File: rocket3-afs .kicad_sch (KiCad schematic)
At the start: 98 parts, among them IC1 ISL85005AFRZ-T7A, J1 ARMING_PLUG, J2 POWER, J3 E-MATCH_DROGUE, J4 SWD, J5 E-MATCH_RECOVERY, M5 MG90S, M6 MG90S, M7 MG90S, M8 MG90s, Q1 Q_NMOS_GSD, Q2 Q_NMOS_GSD, Q3 Q_NMOS_GSD, Q4 Q_NMOS_GSD, Q6 BC547, U2 MP1584EN-LF-Z, U8 USBLC6-2SC6, U9 MMC5983MA, Y1 16MHz

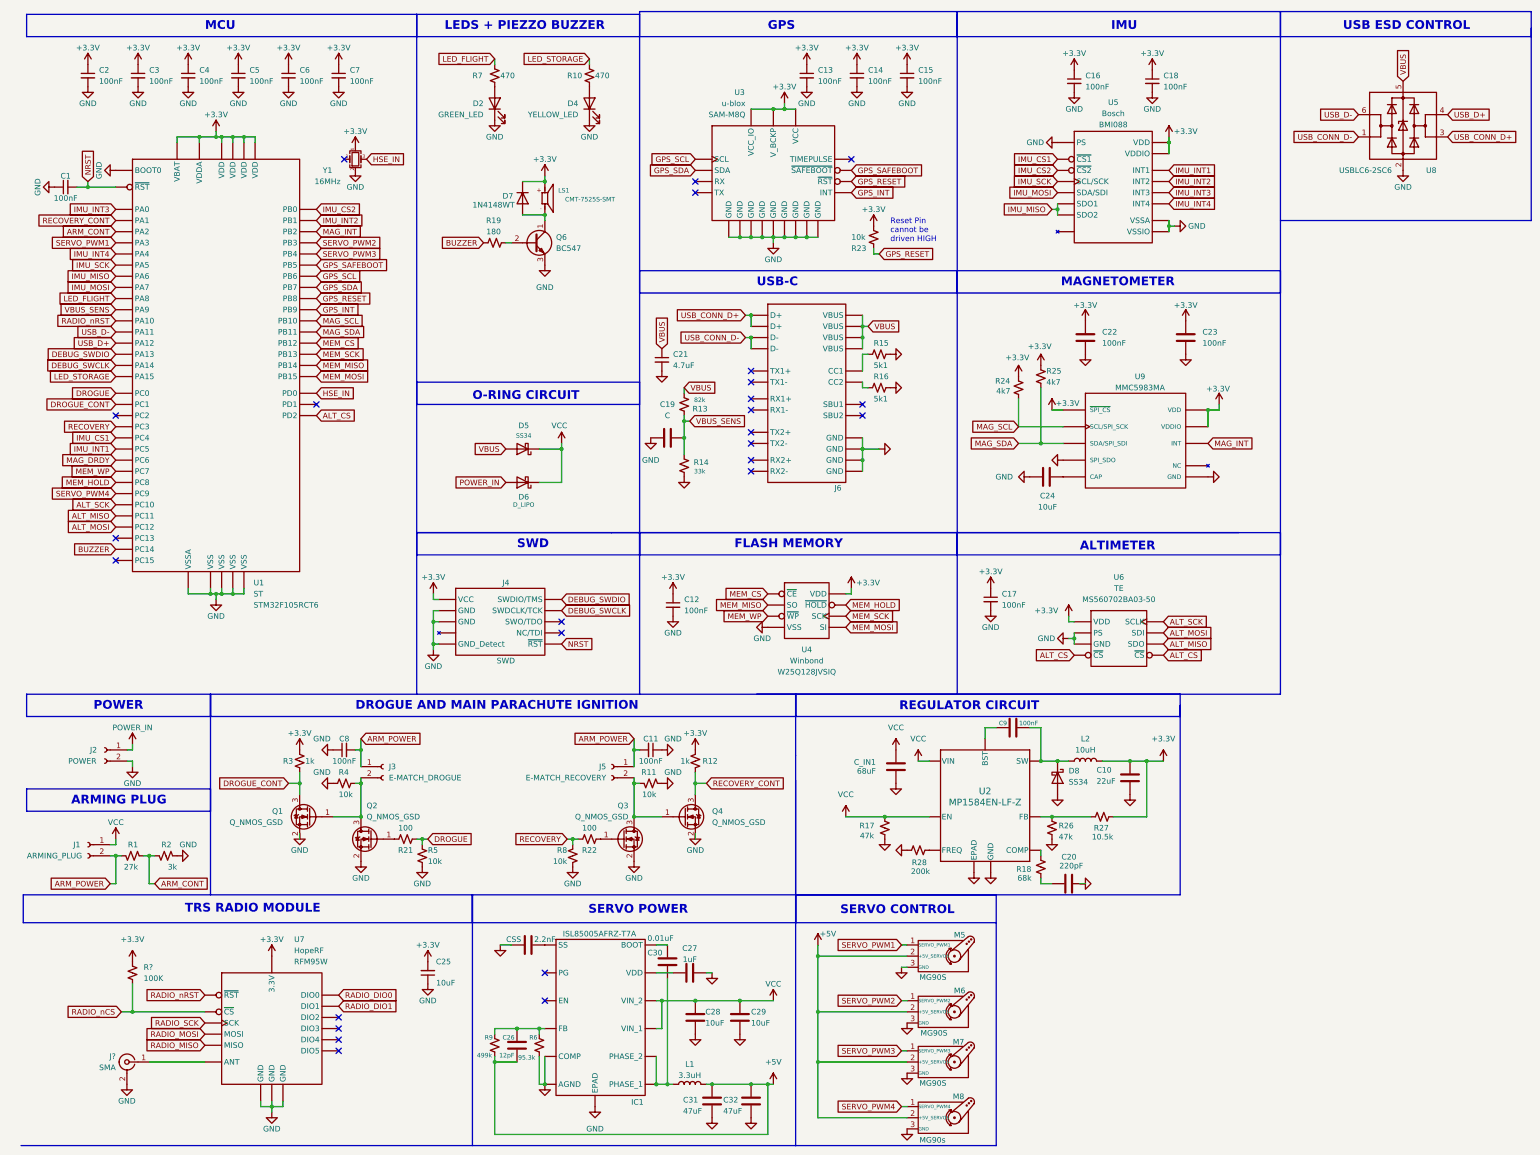
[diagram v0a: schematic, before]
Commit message: servo regulator circuit update
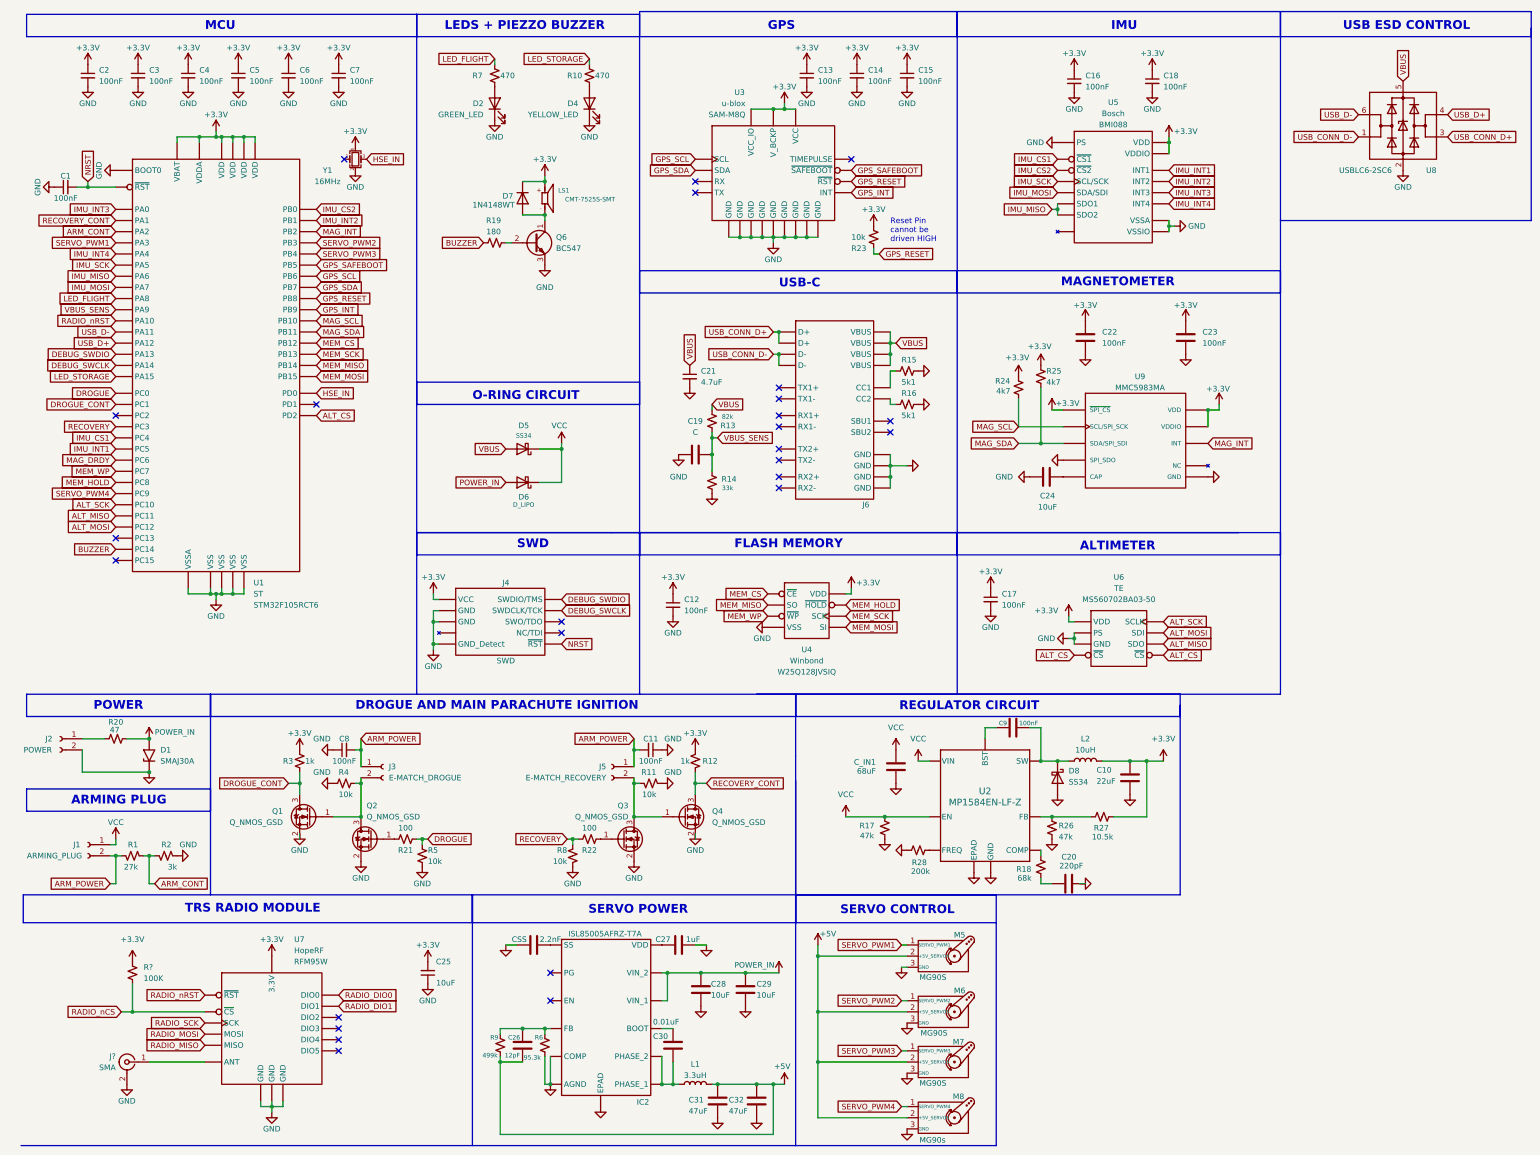
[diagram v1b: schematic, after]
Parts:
- removed IC1: ISL85005AFRZ-T7A, SON50P300X400X90-13N-D, symbol ISL85005AFRZ-T7A:ISL85005AFRZ-T7A
- added D1: SMAJ30A, Diode_SMD:D_SMA, symbol Diode:SMAJ30A
- added IC2: ISL85005AFRZ-T7A, SON50P300X400X90-13N-D, symbol ISL85005AFRZ-T7A:ISL85005AFRZ-T7A
- added R20: 47, symbol Device:R_Small_US
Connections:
- net GND: now also D1.1 (A1), IC2. (PHASE_1)
- net POWER_IN: now also C28.2, C29.2, D1.2 (A2), IC2. (PHASE_1), R20.2; no longer J2.1 (Pin_1)
- net VCC: no longer C28.2, C29.2
- net at C30.2, L1.1: now also IC2. (PHASE_1)
- net at CSS.2: now also IC2. (PHASE_1)
- net at C26.1, R6.1, R9.1: now also IC2. (PHASE_1)
- net at C27.1: now also IC2. (PHASE_1)
- net at C30.1: now also IC2. (PHASE_1)
- new net: J2.1 (Pin_1), R20.1
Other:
- moved on the sheet: C19, C21, J2, J6, R13, R14, R15, R16

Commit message: USB and Lipo power isolation, Regulator circuits fixed, footprints assigned
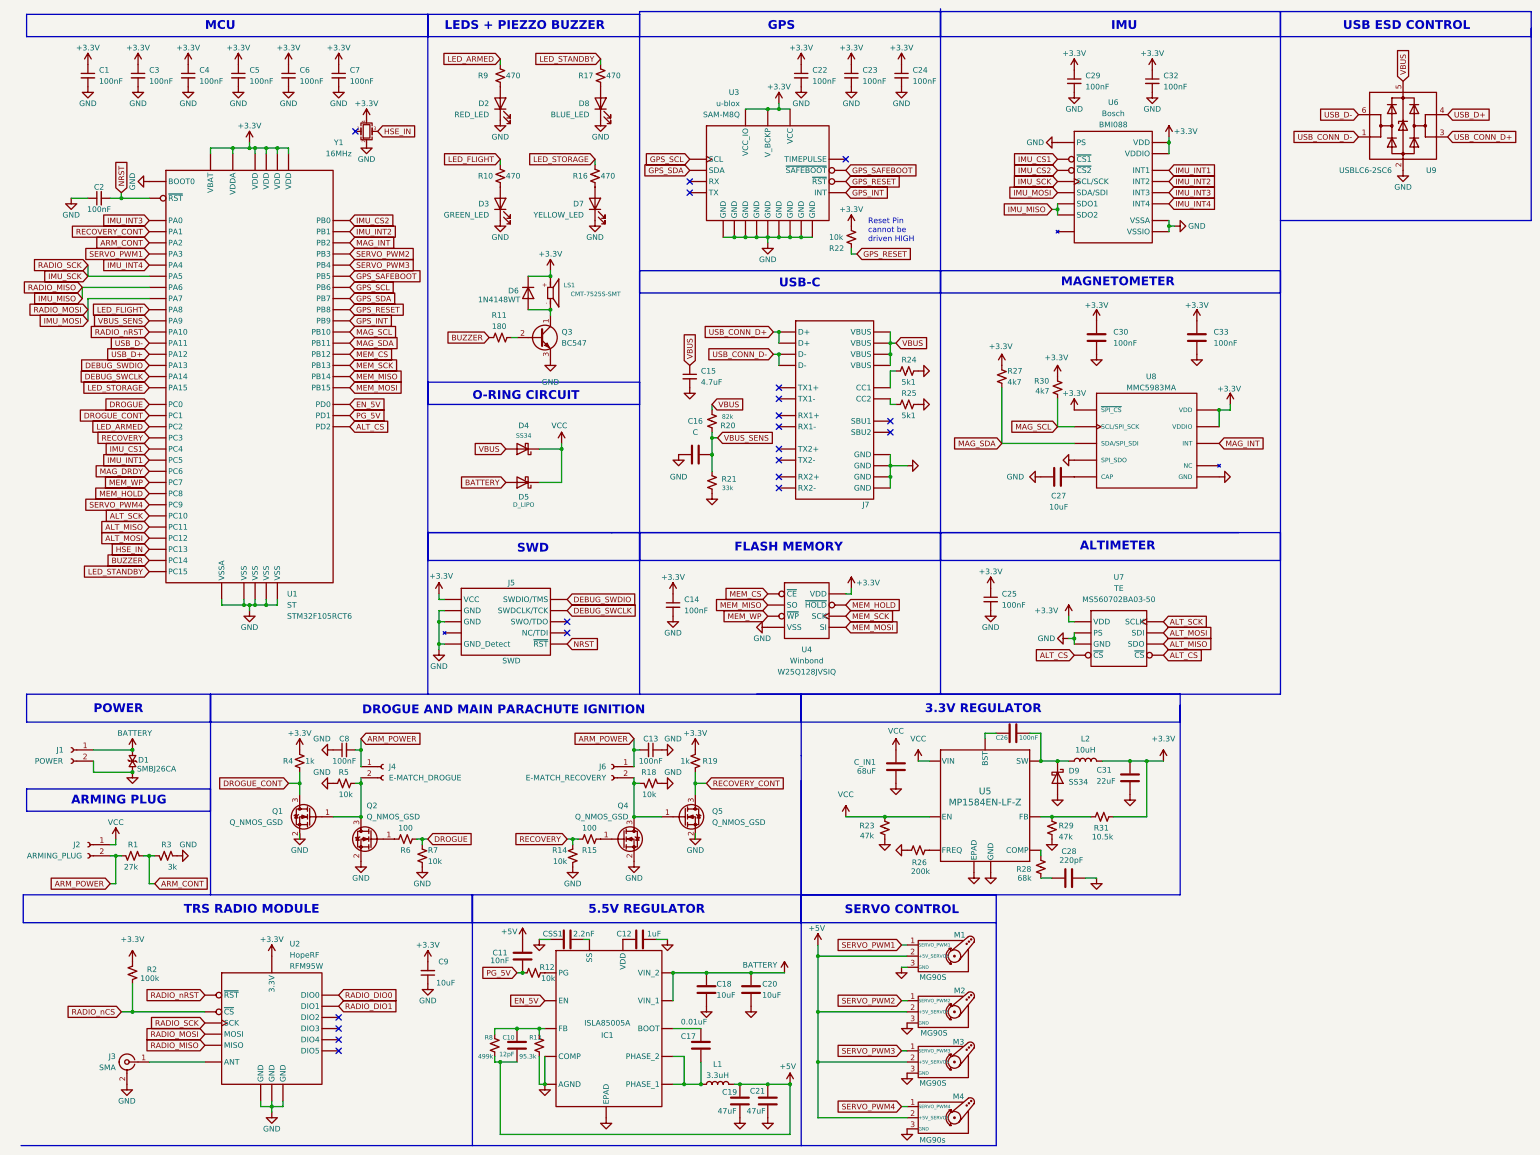
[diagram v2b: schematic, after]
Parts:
- removed D1: SMAJ30A, Diode_SMD:D_SMA, symbol Diode:SMAJ30A
- removed IC2: ISL85005AFRZ-T7A, SON50P300X400X90-13N-D, symbol ISL85005AFRZ-T7A:ISL85005AFRZ-T7A
- removed R20: 47, symbol Device:R_Small_US
- removed R?: 100K, Resistor_SMD:R_0402_1005Metric, symbol Device:R_Small_US
- added C11: 10nF, Capacitor_SMD:C_0603_1608Metric, symbol Device:C
- added D1: SMBJ26CA, 1.0SMBJ28CA-Diotec-Semiconductor-Symbol-Kicad-1_3:P26_DO-214AA_SMB, symbol SMBJ26CA:SMBJ26CA
- added D2: RED_LED, Diode_SMD:D_0603_1608Metric, symbol Device:LED
- added D8: BLUE_LED, Diode_SMD:D_0603_1608Metric, symbol Device:LED
- added IC1: ISLA85005A, KiCad:SON50P300X400X90-13N-D, symbol ISL85005AFRZ-T7A:ISL85005AFRZ-T7A
- added R12: 10k, Resistor_SMD:R_0603_1608Metric, symbol Device:R_Small_US
- added R17, R9: 470, Resistor_SMD:R_0603_1608Metric, symbol Device:R_Small_US
- added R2: 100k, Resistor_SMD:R_0603_1608Metric, symbol Device:R_Small_US
- C10: renamed from C26; footprint (none) -> Capacitor_SMD:C_0603_1608Metric
- C12: renamed from C27; footprint (none) -> Capacitor_SMD:C_0603_1608Metric
- C16: renamed from C19; footprint (none) -> Capacitor_SMD:C_0603_1608Metric
- C17: renamed from C30; footprint (none) -> Capacitor_SMD:C_0603_1608Metric
- C18: renamed from C28; footprint (none) -> Capacitor_SMD:C_0603_1608Metric
- C19: renamed from C31; footprint (none) -> Capacitor_SMD:C_0603_1608Metric
- C20: renamed from C29; footprint (none) -> Capacitor_SMD:C_0603_1608Metric
- C21: renamed from C32; footprint (none) -> Capacitor_SMD:C_0603_1608Metric
- C26: renamed from C9; footprint (none) -> Capacitor_SMD:C_0603_1608Metric
- C27: renamed from C24; footprint (none) -> Capacitor_SMD:C_0603_1608Metric
- C28: renamed from C20; footprint (none) -> Capacitor_SMD:C_0603_1608Metric
- C30: renamed from C22; footprint (none) -> Capacitor_SMD:C_0603_1608Metric
- C31: renamed from C10; footprint (none) -> Capacitor_SMD:C_0603_1608Metric
- C33: renamed from C23; footprint (none) -> Capacitor_SMD:C_0603_1608Metric
- CSS1: renamed from CSS; footprint (none) -> Capacitor_SMD:C_0603_1608Metric
- C_IN1: footprint (none) -> Capacitor_SMD:C_0603_1608Metric
- L1, L2: footprint (none) -> Inductor_SMD:L_0603_1608Metric
- M1: renamed from M5; footprint (none) -> Connector_PinHeader_2.54mm:PinHeader_1x03_P2.54mm_Vertical
- M2: renamed from M6; footprint (none) -> Connector_PinHeader_2.54mm:PinHeader_1x03_P2.54mm_Vertical
- M3: renamed from M7; footprint (none) -> Connector_PinHeader_2.54mm:PinHeader_1x03_P2.54mm_Vertical
- M4: renamed from M8; footprint (none) -> Connector_PinHeader_2.54mm:PinHeader_1x03_P2.54mm_Vertical
- R11: renamed from R19; footprint (none) -> Resistor_SMD:R_0603_1608Metric
- R13: renamed from R6; footprint (none) -> Resistor_SMD:R_0603_1608Metric
- R23: renamed from R17; footprint (none) -> Resistor_SMD:R_0603_1608Metric
- R26: renamed from R28; footprint (none) -> Resistor_SMD:R_0603_1608Metric
- R27: renamed from R25; footprint (none) -> Resistor_SMD:R_0603_1608Metric
- R28: renamed from R18; footprint (none) -> Resistor_SMD:R_0603_1608Metric
- R29: renamed from R26; footprint (none) -> Resistor_SMD:R_0603_1608Metric
- R30: renamed from R24; footprint (none) -> Resistor_SMD:R_0603_1608Metric
- R31: renamed from R27; footprint (none) -> Resistor_SMD:R_0603_1608Metric
- R8: renamed from R9; footprint (none) -> Resistor_SMD:R_0603_1608Metric
- U5: renamed from U2; footprint SOIC8E_MPS -> MP1584EN:SOIC8E_MPS
- gave numbers to parts that had none: 1
- renumbered C2 to C1, C11 to C13, C12 to C14, C21 to C15, C1 to C2, C13 to C22, C14 to C23, C15 to C24, C17 to C25, C16 to C29, C18 to C32, C25 to C9, D2 to D3, D5 to D4, D6 to D5, D7 to D6, D4 to D7, D8 to D9, J2 to J1, J1 to J2, J3 to J4, J4 to J5, J5 to J6, J6 to J7, Q6 to Q3, Q3 to Q4, Q4 to Q5, R7 to R10, R8 to R14, R22 to R15, R10 to R16, R11 to R18, R12 to R19, R13 to R20, R14 to R21, R23 to R22, R15 to R24, R16 to R25, R2 to R3, R3 to R4, R4 to R5, R21 to R6, R5 to R7, U7 to U2, U5 to U6, U6 to U7, U9 to U8, U8 to U9
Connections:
- net POWER_IN is gone; now on net BATTERY: C18.2, C20.2, D5.2 (A)
- net RADIO_MISO is gone; now on net IMU_MISO: U2.2 (MISO)
- net RADIO_MOSI is gone; now on net IMU_MOSI: U2.3 (MOSI)
- net RADIO_SCK is gone; now on net IMU_SCK: U2.4 (SCK)
- net +3.3V: now also R2.2
- net +5V: now also C11.1
- net GND: now also D1., D2.1 (K), D8.1 (K), IC1. (PHASE_1)
- net HSE_IN: now also U1.2 (PC13); no longer U1.5 (PD0)
- net RADIO_nCS: now also R2.1
- net at C10.1, R13.1, R8.1: now also IC1. (PHASE_1)
- net at CSS1.2: now also IC1. (PHASE_1)
- net at C17.2, L1.1: now also IC1. (PHASE_1)
- net BATTERY: now reaches J1.1 (Pin_1)
- net BATTERY: now also D1., IC1. (PHASE_1)
- net at C12.1: now also IC1. (PHASE_1)
- net at C17.1: now also IC1. (PHASE_1)
- net LED_ARMED: now reaches U1.10 (PC2)
- net LED_ARMED: now also R9.1
- net LED_STANDBY: now reaches U1.4 (PC15)
- net LED_STANDBY: now also R17.1
- net PG_5V: now reaches U1.6 (PD1)
- net PG_5V: now also C11.2, R12.1
- new net: D2.2 (A), R9.2
- new net: D8.2 (A), R17.2
- new net: IC1. (PHASE_1), R12.2
- new net EN_5V: IC1. (PHASE_1), U1.5 (PD0)
- no-connect marks 26 -> 20
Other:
- note added: "3.3V REGULATOR"
- note added: "5.5V REGULATOR"
- note removed: "REGULATOR CIRCUIT"
- note removed: "SERVO POWER"
- moved on the sheet: C10, C12, C17, C18, C19, C2, C20, C21, C22, C23, C24, C26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

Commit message: added capacitors for arming plug, 3.3V en pin fixed
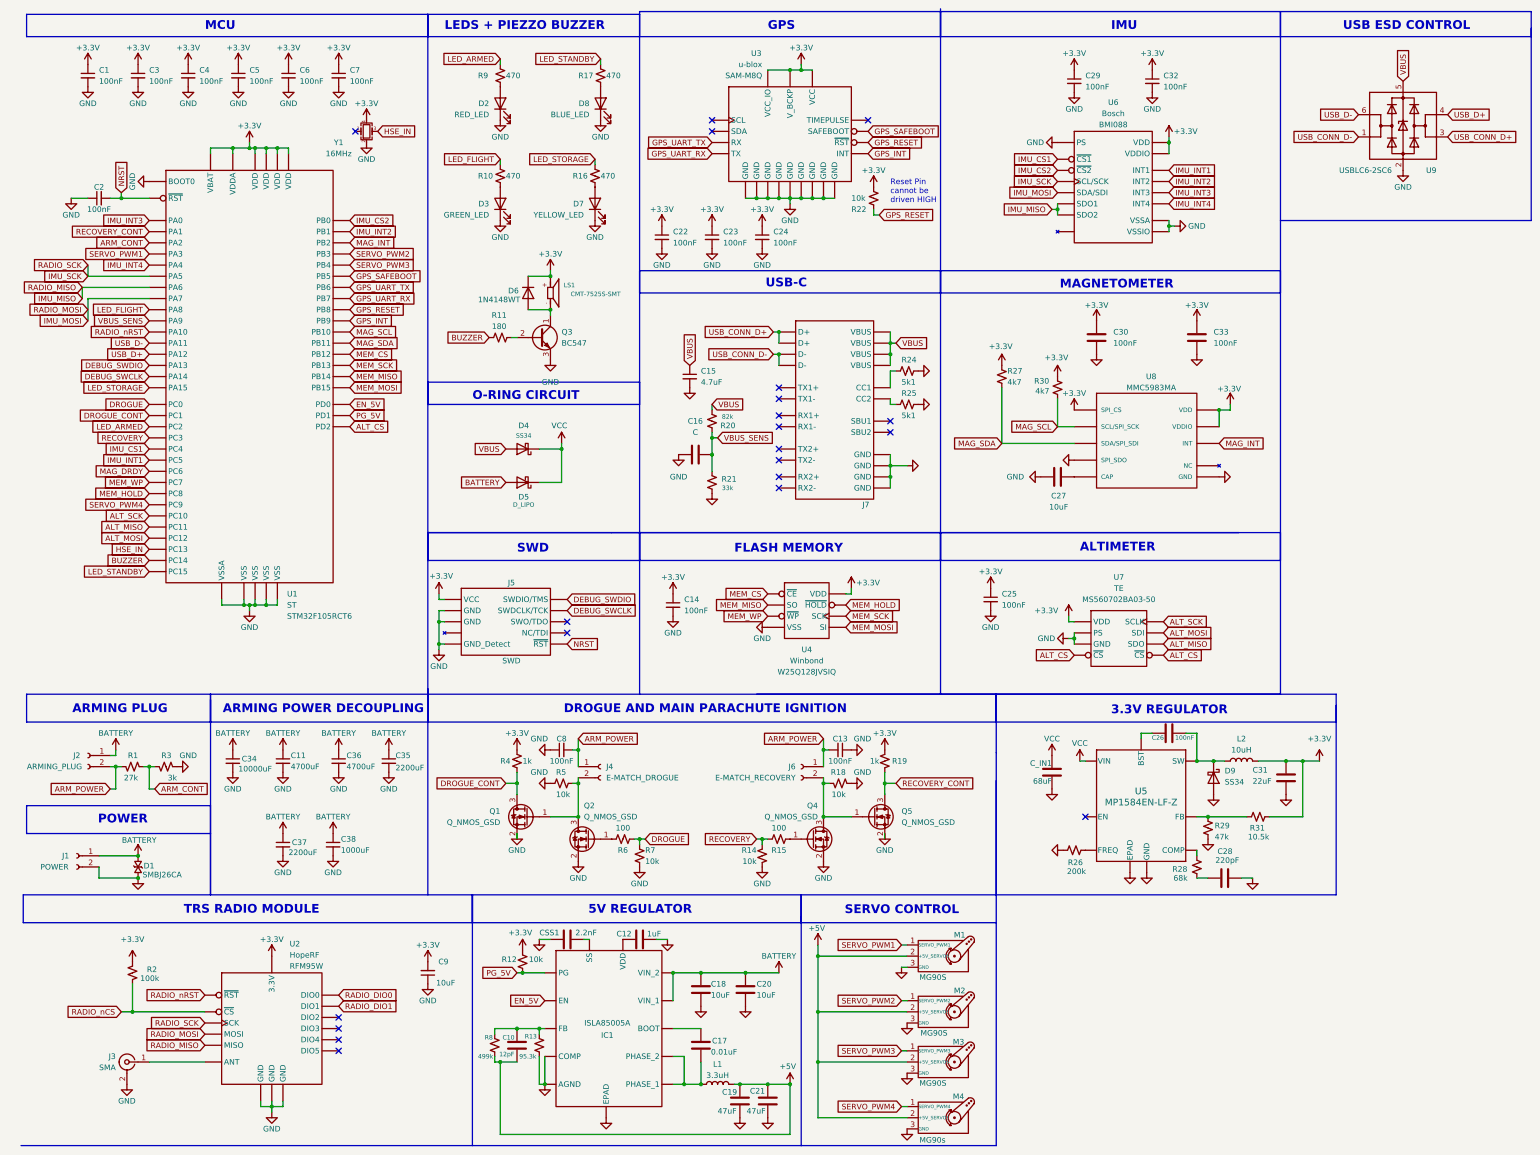
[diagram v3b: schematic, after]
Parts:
- removed C11: 10nF, Capacitor_SMD:C_0603_1608Metric, symbol Device:C
- removed R23: 47k, Resistor_SMD:R_0603_1608Metric, symbol Device:R_Small_US
- added C11, C36: 4700uF, Capacitor_SMD:C_0603_1608Metric, symbol Device:C_Small
- added C34: 10000uF, Capacitor_SMD:C_0603_1608Metric, symbol Device:C_Small
- added C35, C37: 2200uF, Capacitor_SMD:C_0603_1608Metric, symbol Device:C_Small
- added C38: 1000uF, Capacitor_SMD:C_0603_1608Metric, symbol Device:C_Small
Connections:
- net +3.3V: now also R12.2
- net BATTERY: now also J2.1 (Pin_1), C11.1, C34.1, C35.1, C36.1, C37.1, C38.1
- net GND: now also C11.2, C34.2, C35.2, C36.2, C37.2, C38.2
- net PG_5V: now also IC1. (PHASE_1)
- net VCC: no longer J2.1 (Pin_1)
- net GPS_UART_RX: now reaches U3.13 (TX)
- net GPS_UART_RX: now also U1.59 (PB7)
- net GPS_UART_TX: now reaches U3.14 (RX)
- net GPS_UART_TX: now also U1.58 (PB6)
- net GPS_SCL: no longer names the net of U3.12 (SCL)
- net GPS_SCL: no longer U1.58 (PB6)
- net GPS_SDA: no longer names the net of U3.9 (SDA)
- net GPS_SDA: no longer U1.59 (PB7)
- no-connect marks 20 -> 21
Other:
- note added: "5V REGULATOR"
- note added: "ARMING POWER DECOUPLING"
- note removed: "5.5V REGULATOR"
- moved on the sheet: C13, C18, C20, C22, C23, C24, C26, C28, C31, C8, C_IN1, D1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
